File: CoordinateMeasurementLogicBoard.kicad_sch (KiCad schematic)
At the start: 43 parts, among them J1 DE9_Receptacle_MountingHoles, J2 DE9_Receptacle_MountingHoles, J3 DE9_Receptacle_MountingHoles, J4 DE9_Receptacle_MountingHoles, J5 DE9_Receptacle_MountingHoles, Q1 BDP948, Q2 BC856, Q3 BC847, U1 AM2DS-0509SJZ

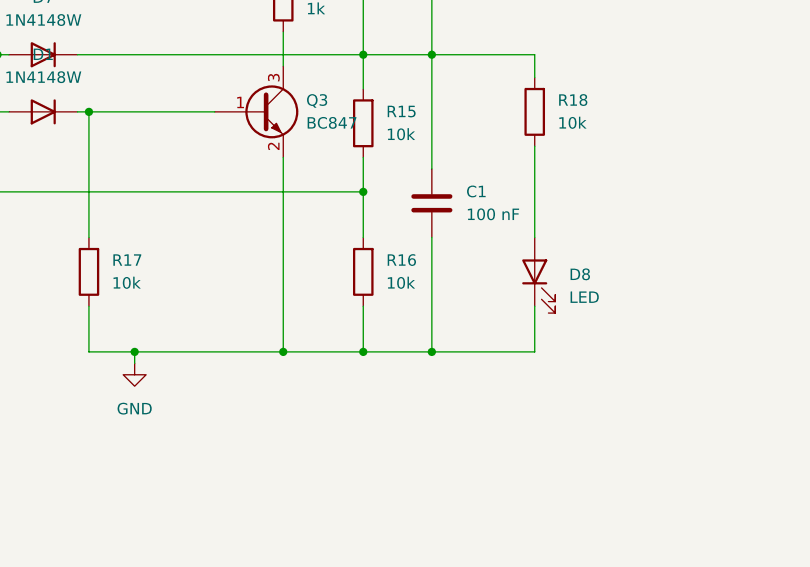
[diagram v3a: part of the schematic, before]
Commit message: fix: R16 wasn't updated correctly
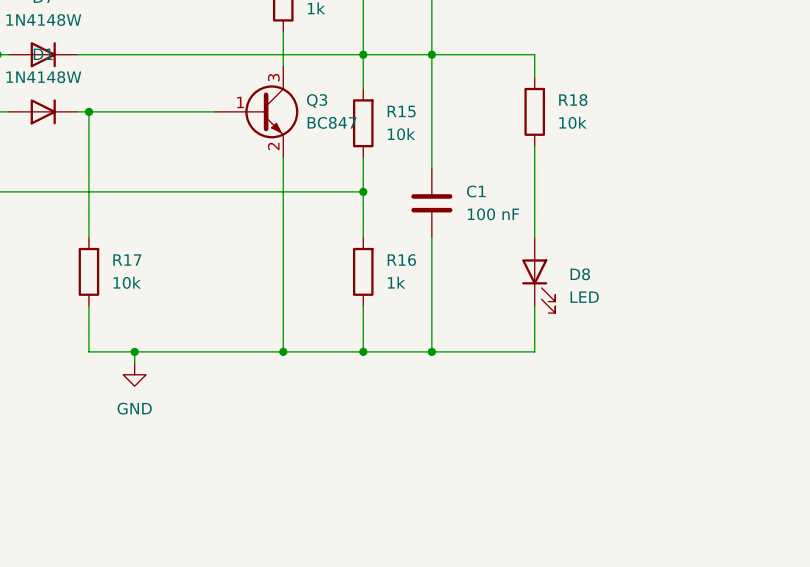
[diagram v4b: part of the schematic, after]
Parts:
- R16: value 10k -> 1k; Reichelt.de SMD-0805 10,0K -> SMD-0805 1,0K
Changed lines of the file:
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@@
 			)
 		)
-		(property "Value" "10k"
+		(property "Value" "1k"
 			(at 172.72 96.5199 0)
 			(effects
@@
 			)
 		)
-		(property "Reichelt.de" "SMD-0805 10,0K"
+		(property "Reichelt.de" "SMD-0805 1,0K"
 			(at 170.18 95.25 0)
 			(effects

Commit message: ready; mounting holes; cosmetic
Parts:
- added H1, H10, H2, H3, H4, H5, H6, H7, H8, H9: MountingHole_Pad, MountingHole:MountingHole_3.2mm_M3_Pad_Via, symbol Mechanical:MountingHole_Pad
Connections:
- net GND: now also H1.1, H10.1, H2.1, H3.1, H4.1, H5.1, H6.1, H7.1, H8.1, H9.1
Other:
- company: (none) -> HTW Dresden
- title: (none) -> Coordinate Measurement Arm Logic Board
- moved on the sheet: D2, D3, D4, D5, D6, J1, J2, J3, J4, J5, R1, R10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

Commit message: replaced D-Sub-9 Connector
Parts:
- J1, J2, J3, J4, J5: footprint Connector_Dsub:DSUB-9_Female_Horizontal_P2.77x2.84mm_EdgePinOffset4.94mm_Housed_MountingHolesOffset7.48mm -> Connector_Dsub:DSUB-9_Socket_Horizontal_P2.77x2.84mm_EdgePinOffset7.70mm_Housed_MountingHolesOffset9.12mm; Reichelt.de D-SUB BU 09US -> D-SUB BU 09EU
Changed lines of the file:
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@@
 (kicad_sch
-	(version 20231120)
+	(version 20250114)
 	(generator "eeschema")
-	(generator_version "8.0")
+	(generator_version "9.0")
 	(paper "A4")
 	(title_block
@@
 	(label "B1"
 		(at 80.01 99.06 0)
-		(fields_autoplaced yes)
 		(effects
 			(font
@@
 	(label "A3"
 		(at 218.44 118.11 0)
-		(fields_autoplaced yes)
 		(effects
 			(font
@@
 	(label "B2"
 		(at 80.01 93.98 0)
-		(fields_autoplaced yes)
 		(effects
 			(font
@@
 	(label "A2"
 		(at 218.44 87.63 0)
-		(fields_autoplaced yes)
 		(effects
 			(font
@@
 	(label "PWR"
 		(at 218.44 52.07 0)
-		(fields_autoplaced yes)
 		(effects
 			(font
@@
 	(label "{A[0..4] B[0..4] PWR}"
 		(at 157.48 22.86 0)
-		(fields_autoplaced yes)
 		(effects
 			(font
@@
 	(label "PWR"
 		(at 189.23 27.94 0)
-		(fields_autoplaced yes)
 		(effects
 			(font
@@
 	(label "A4"
 		(at 80.01 81.28 0)
-		(fields_autoplaced yes)
 		(effects
 			(font
@@
 	(label "A2"
 		(at 80.01 91.44 0)
-		(fields_autoplaced yes)
 		(effects
 			(font
@@
 	(label "PWR"
 		(at 218.44 82.55 0)
-		(fields_autoplaced yes)
 		(effects
 			(font
@@
 	(label "B2"
 		(at 218.44 92.71 0)
-		(fields_autoplaced yes)
 		(effects
 			(font
@@
 	(label "PWR"
 		(at 218.44 113.03 0)
-		(fields_autoplaced yes)
 		(effects
 			(font
@@
 	(label "B0"
 		(at 218.44 31.75 0)
-		(fields_autoplaced yes)
 		(effects
 			(font
@@
 	(label "PWR"
 		(at 218.44 143.51 0)
-		(fields_autoplaced yes)
 		(effects
 			(font
@@
 	(label "PWR"
 		(at 218.44 20.32 0)
-		(fields_autoplaced yes)
 		(effects
 			(font
@@
 	(label "A1"
 		(at 80.01 96.52 0)
-		(fields_autoplaced yes)
 		(effects
 			(font
@@
 	(label "B3"
 		(at 80.01 88.9 0)
-		(fields_autoplaced yes)
 		(effects
 			(font
@@
 	(label "A1"
 		(at 218.44 57.15 0)
-		(fields_autoplaced yes)
 		(effects
 			(font
@@
 	(label "B3"
 		(at 218.44 123.19 0)
-		(fields_autoplaced yes)
 		(effects
 			(font
@@
 	(label "A0"
 		(at 80.01 101.6 0)
-		(fields_autoplaced yes)
 		(effects
 			(font
@@
 	(label "A0"
 		(at 218.44 26.67 0)
-		(fields_autoplaced yes)
 		(effects
 			(font
@@
 	(label "B1"
 		(at 218.44 62.23 0)
-		(fields_autoplaced yes)
 		(effects
 			(font
@@
 	(label "Error_LED"
 		(at 80.01 49.53 0)
-		(fields_autoplaced yes)
 		(effects
 			(font
@@
 	(label "A4"
 		(at 218.44 148.59 0)
-		(fields_autoplaced yes)
 		(effects
 			(font
@@
 	(label "A3"
 		(at 80.01 86.36 0)
-		(fields_autoplaced yes)
 		(effects
 			(font
@@
 	(label "B4"
 		(at 218.44 153.67 0)
-		(fields_autoplaced yes)
 		(effects
 			(font
@@
 	(label "B4"
 		(at 80.01 83.82 0)
-		(fields_autoplaced yes)
 		(effects
 			(font
@@
 	(label "B0"
 		(at 80.01 104.14 0)
-		(fields_autoplaced yes)
 		(effects
 			(font
@@
 			)
 		)
-		(property "Footprint" "Connector_Dsub:DSUB-9_Female_Horizontal_P2.77x2.84mm_EdgePinOffset4.94mm_Housed_MountingHolesOffset7.48mm"
+		(property "Footprint" "Connector_Dsub:DSUB-9_Socket_Horizontal_P2.77x2.84mm_EdgePinOffset7.70mm_Housed_MountingHolesOffset9.12mm"
 			(at 247.65 59.69 0)
 			(effects
@@
 			)
 		)
-		(property "Reichelt.de" "D-SUB BU 09US"
+		(property "Reichelt.de" "D-SUB BU 09EU"
 			(at 247.65 59.69 0)
 			(effects
@@
 			)
 		)
-		(property "Footprint" "Connector_Dsub:DSUB-9_Female_Horizontal_P2.77x2.84mm_EdgePinOffset4.94mm_Housed_MountingHolesOffset7.48mm"
+		(property "Footprint" "Connector_Dsub:DSUB-9_Socket_Horizontal_P2.77x2.84mm_EdgePinOffset7.70mm_Housed_MountingHolesOffset9.12mm"
 			(at 247.65 29.21 0)
 			(effects
@@
 			)
 		)
-		(property "Reichelt.de" "D-SUB BU 09US"
+		(property "Reichelt.de" "D-SUB BU 09EU"
 			(at 247.65 29.21 0)
 			(effects
@@
 			)
 		)
-		(property "Footprint" "Connector_Dsub:DSUB-9_Female_Horizontal_P2.77x2.84mm_EdgePinOffset4.94mm_Housed_MountingHolesOffset7.48mm"
+		(property "Footprint" "Connector_Dsub:DSUB-9_Socket_Horizontal_P2.77x2.84mm_EdgePinOffset7.70mm_Housed_MountingHolesOffset9.12mm"
 			(at 247.65 151.13 0)
 			(effects
@@
 			)
 		)
-		(property "Reichelt.de" "D-SUB BU 09US"
+		(property "Reichelt.de" "D-SUB BU 09EU"
 			(at 247.65 151.13 0)
 			(effects
@@
 			)
 		)
-		(property "Footprint" "Connector_Dsub:DSUB-9_Female_Horizontal_P2.77x2.84mm_EdgePinOffset4.94mm_Housed_MountingHolesOffset7.48mm"
+		(property "Footprint" "Connector_Dsub:DSUB-9_Socket_Horizontal_P2.77x2.84mm_EdgePinOffset7.70mm_Housed_MountingHolesOffset9.12mm"
 			(at 247.65 120.65 0)
 			(effects
@@
 			)
 		)
-		(property "Reichelt.de" "D-SUB BU 09US"
+		(property "Reichelt.de" "D-SUB BU 09EU"
 			(at 247.65 120.65 0)
 			(effects
@@
 			)
 		)
-		(property "Footprint" "Connector_Dsub:DSUB-9_Female_Horizontal_P2.77x2.84mm_EdgePinOffset4.94mm_Housed_MountingHolesOffset7.48mm"
+		(property "Footprint" "Connector_Dsub:DSUB-9_Socket_Horizontal_P2.77x2.84mm_EdgePinOffset7.70mm_Housed_MountingHolesOffset9.12mm"
 			(at 247.65 90.17 0)
 			(effects
@@
 			)
 		)
-		(property "Reichelt.de" "D-SUB BU 09US"
+		(property "Reichelt.de" "D-SUB BU 09EU"
 			(at 247.65 90.17 0)
 			(effects
@@
 		)
 	)
+	(embedded_fonts no)
 )
